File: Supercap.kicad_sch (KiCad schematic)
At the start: 2 parts

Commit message: more simulation work + fixed some things in root schematic
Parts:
- added V_{MiniPC}: Conn_01x02_Pin, symbol Connector:Conn_01x02_Pin
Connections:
- net Housekeeping/MiniPC: now also V_{MiniPC}.1 (Pin_1)
- new net GND: V_{MiniPC}.2 (Pin_2)
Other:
- sheet Control ports: added none; removed SCL_{IN}, SDA_{IN}
- sheet Housekeeping ports: added +12V; removed +5V
- sheet Voltage Converter ports: added +12V; removed +10V
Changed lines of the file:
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@@
-	)
-	(junction
-		(at 86.36 80.01)
-		(diameter 0)
-		(color 0 0 0 0)
 	)
 	(junction
@@
 		)
 	)
+	(wire
+		(pts
+			(xy 137.16 71.12) (xy 137.16 82.55)
+		)
+		(stroke
+			(width 0)
+			(type default)
+		)
+	)
 	(polyline
 		(pts
@@
 		)
 	)
+	(wire
+		(pts
+			(xy 35.56 82.55) (xy 35.56 85.09)
+		)
+		(stroke
+			(width 0)
+			(type default)
+		)
+	)
 	(polyline
 		(pts
@@
 	(wire
 		(pts
-			(xy 86.36 80.01) (xy 88.9 80.01)
+			(xy 82.55 82.55) (xy 88.9 82.55)
 		)
 		(stroke
@@
 	(wire
 		(pts
-			(xy 83.82 83.82) (xy 82.55 83.82)
-		)
-		(stroke
-			(width 0)
-			(type default)
-		)
-	)
-	(wire
-		(pts
 			(xy 205.74 57.15) (xy 205.74 60.96)
 		)
@@
 		)
 	)
+	(wire
+		(pts
+			(xy 33.02 80.01) (xy 40.64 80.01)
+		)
+		(stroke
+			(width 0)
+			(type default)
+		)
+	)
 	(polyline
 		(pts
@@
 	(wire
 		(pts
-			(xy 134.62 73.66) (xy 86.36 73.66)
-		)
-		(stroke
-			(width 0)
-			(type default)
-		)
-	)
-	(wire
-		(pts
-			(xy 82.55 80.01) (xy 86.36 80.01)
-		)
-		(stroke
-			(width 0)
-			(type default)
-		)
-	)
-	(wire
-		(pts
 			(xy 63.5 54.61) (xy 138.43 54.61)
 		)
@@
 		)
 	)
+	(wire
+		(pts
+			(xy 137.16 82.55) (xy 142.24 82.55)
+		)
+		(stroke
+			(width 0)
+			(type default)
+		)
+	)
 	(polyline
 		(pts
@@
 		)
 	)
+	(wire
+		(pts
+			(xy 33.02 82.55) (xy 35.56 82.55)
+		)
+		(stroke
+			(width 0)
+			(type default)
+		)
+	)
 	(polyline
 		(pts
@@
 		)
 	)
-	(wire
-		(pts
-			(xy 86.36 73.66) (xy 86.36 80.01)
-		)
-		(stroke
-			(width 0)
-			(type default)
-		)
-	)
 	(polyline
 		(pts
@@
 		)
 	)
+	(wire
+		(pts
+			(xy 85.09 71.12) (xy 137.16 71.12)
+		)
+		(stroke
+			(width 0)
+			(type default)
+		)
+	)
+	(wire
+		(pts
+			(xy 85.09 80.01) (xy 85.09 71.12)
+		)
+		(stroke
+			(width 0)
+			(type default)
+		)
+	)
+	(wire
+		(pts
+			(xy 82.55 80.01) (xy 85.09 80.01)
+		)
+		(stroke
+			(width 0)
+			(type default)
+		)
+	)
 	(polyline
 		(pts
@@
 			(width 0)
 			(type default)
-		)
-	)
-	(label "+5V"
-		(at 83.82 83.82 0)
-		(effects
-			(font
-				(size 1.27 1.27)
-			)
-			(justify left bottom)
 		)
 	)
@@
 	(symbol
 		(lib_id "Connector:Conn_01x02_Pin")
+		(at 27.94 80.01 0)
+		(unit 1)
+		(exclude_from_sim no)
+		(in_bom yes)
+		(on_board yes)
+		(dnp no)
+		(property "Reference" "V_{MiniPC}"
+			(at 19.685 79.756 0)
+			(effects
+				(font
+					(size 1.27 1.27)
+				)
+			)
+		)
+		(property "Value" "Conn_01x02_Pin"
+			(at 19.685 82.296 0)
+			(effects
+				(font
+					(size 1.27 1.27)
+				)
+			)
+		)
+		(property "Footprint" ""
+			(at 27.94 80.01 0)
+			(effects
+				(font
+					(size 1.27 1.27)
+				)
+				(hide yes)
+			)
+		)
+		(property "Datasheet" "~"
+			(at 27.94 80.01 0)
+			(effects
+				(font
+					(size 1.27 1.27)
+				)
+				(hide yes)
+			)
+		)
+		(property "Description" "Generic connector, single row, 01x02, script generated"
+			(at 27.94 80.01 0)
+			(effects
+				(font
+					(size 1.27 1.27)
+				)
+				(hide yes)
+			)
+		)
+		(pin "2"
+		)
+		(pin "1"
+		)
+		(instances
+			(project "Supercap"
+				(path "/98ee8313-37ab-4329-91ab-b5710476f82f"
+					(reference "V_{MiniPC}")
+					(unit 1)
+				)
+			)
+		)
+	)
+	(symbol
+		(lib_id "Connector:Conn_01x02_Pin")
 		(at 58.42 54.61 0)
 		(unit 1)
@@
 		)
 	)
+	(symbol
+		(lib_id "power:GND")
+		(at 35.56 85.09 0)
+		(unit 1)
+		(exclude_from_sim no)
+		(in_bom yes)
+		(on_board yes)
+		(dnp no)
+		(fields_autoplaced yes)
+		(property "Reference" "#PWR012"
+			(at 35.56 91.44 0)
+			(effects
+				(font
+					(size 1.27 1.27)
+				)
+				(hide yes)
+			)
+		)
+		(property "Value" "GND"
+			(at 35.56 90.17 0)
+			(effects
+				(font
+					(size 1.27 1.27)
+				)
+			)
+		)
+		(property "Footprint" ""
+			(at 35.56 85.09 0)
+			(effects
+				(font
+					(size 1.27 1.27)
+				)
+				(hide yes)
+			)
+		)
+		(property "Datasheet" ""
+			(at 35.56 85.09 0)
+			(effects
+				(font
+					(size 1.27 1.27)
+				)
+				(hide yes)
+			)
+		)
+		(property "Description" "Power symbol creates a global label with name \"GND\" , ground"
+			(at 35.56 85.09 0)
+			(effects
+				(font
+					(size 1.27 1.27)
+				)
+				(hide yes)
+			)
+		)
+		(pin "1"
+		)
+		(instances
+			(project ""
+				(path "/98ee8313-37ab-4329-91ab-b5710476f82f"
+					(reference "#PWR012")
+					(unit 1)
+				)
+			)
+		)
+	)
 	(sheet
 		(at 40.64 77.47)
@@
 		)
 		(pin "+3V3" output
+			(at 82.55 82.55 0)
+			(effects
+				(font
+					(size 1.27 1.27)
+				)
+				(justify right)
+			)
+		)
+		(pin "+12V" output
 			(at 82.55 80.01 0)
-			(effects
-				(font
-					(size 1.27 1.27)
-				)
-				(justify right)
-			)
-		)
-		(pin "+5V" output
-			(at 82.55 83.82 0)
 			(effects
 				(font
@@
 			)
 		)
-		(pin "+10V" input
+		(pin "+12V" input
 			(at 142.24 82.55 180)
 			(effects
@@
 			)
 		)
-		(pin "SDA_{IN}" bidirectional
-			(at 88.9 100.33 180)
-			(effects
-				(font
-					(size 1.27 1.27)
-				)
-				(justify left)
-			)
-		)
 		(pin "+3V3" input
-			(at 88.9 80.01 180)
-			(effects
-				(font
-					(size 1.27 1.27)
-				)
-				(justify left)
-			)
-		)
-		(pin "SCL_{IN}" input
-			(at 88.9 96.52 180)
-			(effects
-				(font
+			(at 88.9 82.55 180)
+			(effects
+				(font

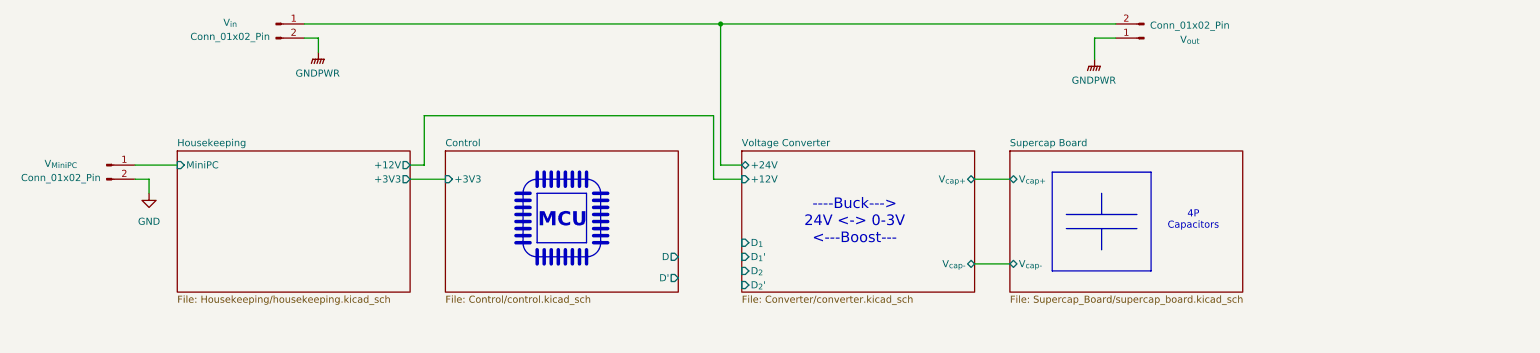
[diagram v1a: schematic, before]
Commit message: wiring connected, now only need msmp0 pinout and footprint assignments
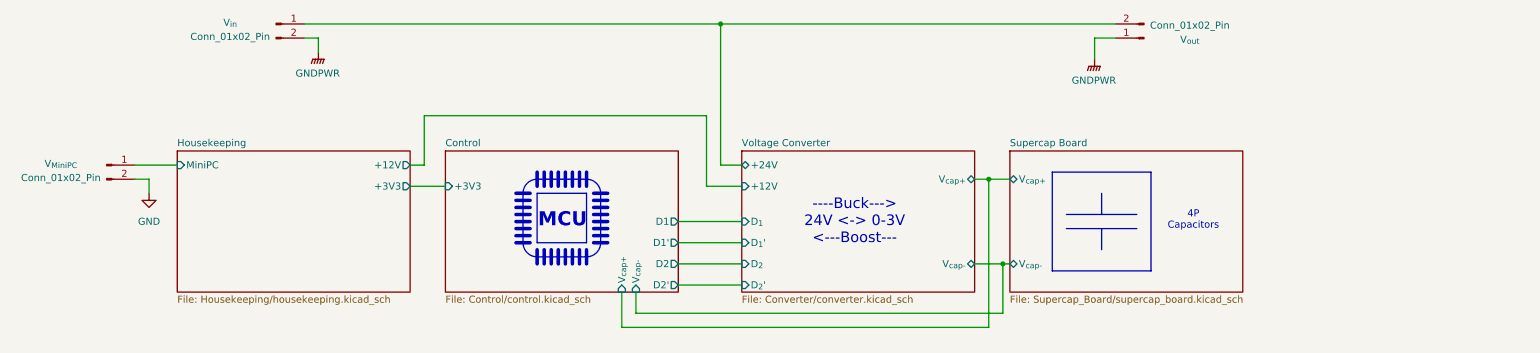
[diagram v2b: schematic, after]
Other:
- sheet Control ports: added D1, D1', D2, D2', V_{cap+}, V_{cap-}; removed D, D'
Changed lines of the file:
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@@
+	)
+	(junction
+		(at 186.69 82.55)
+		(diameter 0)
+		(color 0 0 0 0)
+	)
+	(junction
+		(at 189.23 97.79)
+		(diameter 0)
+		(color 0 0 0 0)
 	)
 	(junction
@@
 		(color 0 0 0 0)
 	)
+	(wire
+		(pts
+			(xy 120.65 102.87) (xy 120.65 109.22)
+		)
+		(stroke
+			(width 0)
+			(type default)
+		)
+	)
 	(polyline
 		(pts
@@
 	(wire
 		(pts
+			(xy 186.69 109.22) (xy 186.69 82.55)
+		)
+		(stroke
+			(width 0)
+			(type default)
+		)
+	)
+	(wire
+		(pts
 			(xy 209.55 57.15) (xy 205.74 57.15)
 		)
@@
 	(wire
 		(pts
-			(xy 137.16 71.12) (xy 137.16 82.55)
+			(xy 135.89 71.12) (xy 135.89 83.82)
 		)
 		(stroke
@@
 	(wire
 		(pts
-			(xy 82.55 82.55) (xy 88.9 82.55)
+			(xy 82.55 83.82) (xy 88.9 83.82)
 		)
 		(stroke
@@
 	(wire
 		(pts
+			(xy 130.81 90.17) (xy 142.24 90.17)
+		)
+		(stroke
+			(width 0)
+			(type default)
+		)
+	)
+	(wire
+		(pts
+			(xy 130.81 97.79) (xy 142.24 97.79)
+		)
+		(stroke
+			(width 0)
+			(type default)
+		)
+	)
+	(wire
+		(pts
 			(xy 205.74 57.15) (xy 205.74 60.96)
 		)
@@
 		)
 	)
+	(wire
+		(pts
+			(xy 120.65 109.22) (xy 186.69 109.22)
+		)
+		(stroke
+			(width 0)
+			(type default)
+		)
+	)
 	(polyline
 		(pts
@@
 		)
 	)
+	(wire
+		(pts
+			(xy 123.19 106.68) (xy 189.23 106.68)
+		)
+		(stroke
+			(width 0)
+			(type default)
+		)
+	)
 	(polyline
 		(pts
@@
 	(wire
 		(pts
-			(xy 184.15 97.79) (xy 190.5 97.79)
+			(xy 184.15 97.79) (xy 189.23 97.79)
 		)
 		(stroke
@@
 	(wire
 		(pts
-			(xy 137.16 82.55) (xy 142.24 82.55)
+			(xy 135.89 83.82) (xy 142.24 83.82)
 		)
 		(stroke
@@
 	(wire
 		(pts
-			(xy 184.15 82.55) (xy 190.5 82.55)
+			(xy 184.15 82.55) (xy 186.69 82.55)
 		)
 		(stroke
@@
 		)
 	)
+	(wire
+		(pts
+			(xy 123.19 102.87) (xy 123.19 106.68)
+		)
+		(stroke
+			(width 0)
+			(type default)
+		)
+	)
 	(polyline
 		(pts
@@
 		)
 	)
+	(wire
+		(pts
+			(xy 130.81 101.6) (xy 142.24 101.6)
+		)
+		(stroke
+			(width 0)
+			(type default)
+		)
+	)
 	(polyline
 		(pts
@@
 		)
 	)
+	(wire
+		(pts
+			(xy 130.81 93.98) (xy 142.24 93.98)
+		)
+		(stroke
+			(width 0)
+			(type default)
+		)
+	)
+	(wire
+		(pts
+			(xy 189.23 106.68) (xy 189.23 97.79)
+		)
+		(stroke
+			(width 0)
+			(type default)
+		)
+	)
 	(polyline
 		(pts
@@
 	(wire
 		(pts
+			(xy 186.69 82.55) (xy 190.5 82.55)
+		)
+		(stroke
+			(width 0)
+			(type default)
+		)
+	)
+	(wire
+		(pts
 			(xy 33.02 82.55) (xy 35.56 82.55)
 		)
@@
 	(wire
 		(pts
-			(xy 85.09 71.12) (xy 137.16 71.12)
+			(xy 85.09 71.12) (xy 135.89 71.12)
 		)
 		(stroke
@@
 		(pts
 			(xy 138.43 54.61) (xy 209.55 54.61)
+		)
+		(stroke
+			(width 0)
+			(type default)
+		)
+	)
+	(wire
+		(pts
+			(xy 189.23 97.79) (xy 190.5 97.79)
 		)
 		(stroke
@@
 		)
 		(pin "+3V3" output
-			(at 82.55 82.55 0)
+			(at 82.55 83.82 0)
 			(effects
 				(font
@@
 		)
 		(pin "+12V" input
-			(at 142.24 82.55 180)
+			(at 142.24 83.82 180)
 			(effects
 				(font
@@
 		)
 		(pin "D_{1}" input
+			(at 142.24 90.17 180)
+			(effects
+				(font
+					(size 1.27 1.27)
+				)
+				(justify left)
+			)
+		)
+		(pin "D_{1}'" input
 			(at 142.24 93.98 180)
 			(effects
@@
 			)
 		)
-		(pin "D_{1}'" input
-			(at 142.24 96.52 180)
-			(effects
-				(font
-					(size 1.27 1.27)
-				)
-				(justify left)
-			)
-		)
 		(pin "D_{2}" input
-			(at 142.24 99.06 180)
+			(at 142.24 97.79 180)
 			(effects
 				(font
@@
 		)
 		(pin "+3V3" input
-			(at 88.9 82.55 180)
+			(at 88.9 83.82 180)
 			(effects
 				(font
@@
 			)
 		)
-		(pin "D" output
-			(at 130.81 96.52 0)
+		(pin "D1" output
+			(at 130.81 90.17 0)
 			(effects
 				(font
@@
 			)
 		)
-		(pin "D'" output
-			(at 130.81 100.33 0)
+		(pin "D1'" output
+			(at 130.81 93.98 0)
 			(effects
 				(font
@@
 			)
 		)
+		(pin "D2" output
+			(at 130.81 97.79 0)
+			(effects
+				(font
+					(size 1.27 1.27)
+				)
+				(justify right)
+			)
+		)
+		(pin "D2'" output
+			(at 130.81 101.6 0)
+			(effects
+				(font
+					(size 1.27 1.27)
+				)
+				(justify right)
+			)
+		)
+		(pin "V_{cap+}" input
+			(at 120.65 102.87 270)
+			(effects
+				(font
+					(size 1.27 1.27)
+				)
+				(justify left)
+			)
+		)
+		(pin "V_{cap-}" input
+			(at 123.19 102.87 270)
+			(effects
+				(font
+					(size 1.27 1.27)
+				)
+				(justify left)
+			)
+		)

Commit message: removed v1 files and assigned mouser part numbers
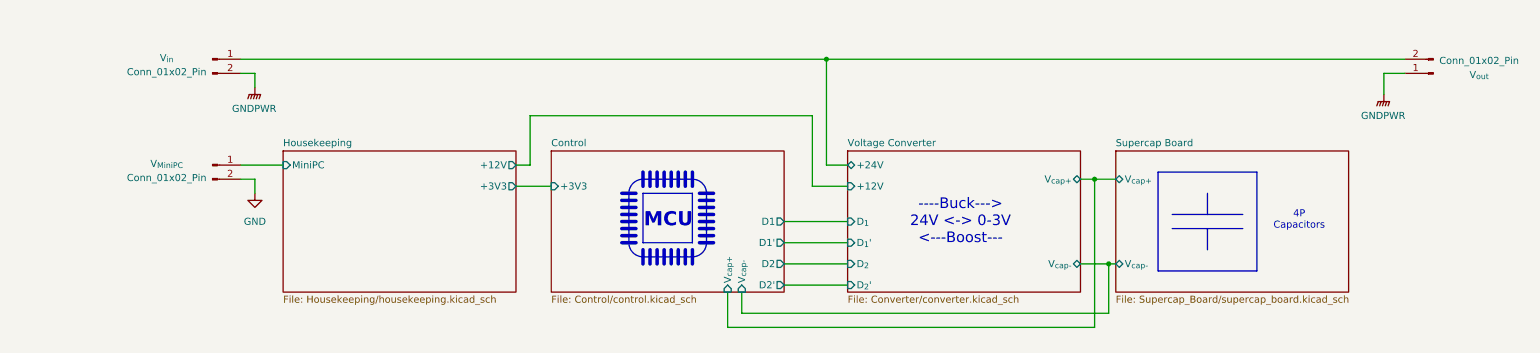
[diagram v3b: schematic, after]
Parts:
- V_{MiniPC}, V_{in}, V_{out}: footprint (none) -> Connector_AMASS:AMASS_XT30U-F_1x02_P5.0mm_Vertical; now left out of the parts list
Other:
- moved on the sheet: V_{MiniPC}, V_{in}, V_{out}

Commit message: began layout
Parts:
- renumbered V_{MiniPC} to V_{MiniPC}1, V_{in} to V_{in}1, V_{out} to V_{out}1
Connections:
- net Voltage Converter/+24V renamed Control/I_{bat,in+}
- net Control/I_{bat,in+}: no longer V_{out}1.2 (Pin_2)
- new net Control/I_{bat,out+}: V_{out}1.2 (Pin_2)
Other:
- sheet Control ports: added I_{L,out+}, I_{bat,in+}, I_{bat,out+}, V_{sc,+}, V_{sc,-}; removed V_{cap+}, V_{cap-}
- moved on the sheet: V_{MiniPC}1, V_{in}1, V_{out}1

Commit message: mostly done with first order layout
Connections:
- net Control/I_{bat,in+}: now also V_{in}1.2 (Pin_2); no longer V_{in}1.1 (Pin_1)
- net GNDPWR: now also V_{in}1.1 (Pin_1); no longer V_{in}1.2 (Pin_2)
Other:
- sheet Housekeeping ports: added +24V; removed none
- company: (none) -> UT Robomaster
- moved on the sheet: V_{MiniPC}1
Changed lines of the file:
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@@
 	(generator_version "9.0")
 	(paper "A4")
+	(title_block
+		(company "UT Robomaster")
+		(comment 1 "Robomaster")
+	)
 	(arc
 		(start 119.38 96.52)
@@
 	)
 	(junction
+		(at 67.31 60.96)
+		(diameter 0)
+		(color 0 0 0 0)
+	)
+	(junction
 		(at 205.74 97.79)
 		(diameter 0)
@@
 	(wire
 		(pts
-			(xy 59.69 60.96) (xy 97.79 60.96)
+			(xy 59.69 60.96) (xy 67.31 60.96)
 		)
 		(stroke
@@
 	(wire
 		(pts
-			(xy 45.72 82.55) (xy 45.72 85.09)
+			(xy 45.72 85.09) (xy 45.72 87.63)
 		)
 		(stroke
@@
 	(wire
 		(pts
-			(xy 43.18 80.01) (xy 50.8 80.01)
+			(xy 43.18 82.55) (xy 50.8 82.55)
+		)
+		(stroke
+			(width 0)
+			(type default)
+		)
+	)
+	(wire
+		(pts
+			(xy 50.8 80.01) (xy 48.26 80.01)
 		)
 		(stroke
@@
 		)
 	)
+	(wire
+		(pts
+			(xy 67.31 60.96) (xy 97.79 60.96)
+		)
+		(stroke
+			(width 0)
+			(type default)
+		)
+	)
 	(polyline
 		(pts
@@
 		)
 	)
+	(wire
+		(pts
+			(xy 48.26 73.66) (xy 67.31 73.66)
+		)
+		(stroke
+			(width 0)
+			(type default)
+		)
+	)
 	(polyline
 		(pts
@@
 	(wire
 		(pts
+			(xy 67.31 60.96) (xy 67.31 73.66)
+		)
+		(stroke
+			(width 0)
+			(type default)
+		)
+	)
+	(wire
+		(pts
 			(xy 205.74 97.79) (xy 208.28 97.79)
 		)
@@
 	(wire
 		(pts
-			(xy 43.18 82.55) (xy 45.72 82.55)
+			(xy 43.18 85.09) (xy 45.72 85.09)
 		)
 		(stroke
@@
 		(pts
 			(xy 144.78 100.33) (xy 148.59 100.33)
+		)
+		(stroke
+			(width 0)
+			(type default)
+		)
+	)
+	(wire
+		(pts
+			(xy 48.26 80.01) (xy 48.26 73.66)
 		)
 		(stroke
@@
 	(symbol
 		(lib_id "Connector:Conn_01x02_Pin")
-		(at 38.1 80.01 0)
+		(at 38.1 82.55 0)
 		(unit 1)
 		(exclude_from_sim no)
@@
 		(dnp no)
 		(property "Reference" "V_{MiniPC}1"
-			(at 29.845 79.756 0)
+			(at 29.845 82.296 0)
 			(effects
 				(font
@@
 		)
 		(property "Value" "Conn_01x02_Pin"
-			(at 29.845 82.296 0)
+			(at 29.845 84.836 0)
 			(effects
 				(font
@@
 		)
 		(property "Footprint" "Connector_AMASS:AMASS_XT30U-F_1x02_P5.0mm_Vertical"
-			(at 38.1 80.01 0)
+			(at 38.1 82.55 0)
 			(effects
 				(font
@@
 		)
 		(property "Datasheet" "~"
-			(at 38.1 80.01 0)
+			(at 38.1 82.55 0)
 			(effects
 				(font
@@
 		)
 		(property "Description" "Generic connector, single row, 01x02, script generated"
-			(at 38.1 80.01 0)
+			(at 38.1 82.55 0)
 			(effects
 				(font
@@
 	(symbol
 		(lib_id "Connector:Conn_01x02_Pin")
-		(at 54.61 60.96 0)
+		(at 54.61 63.5 0)
+		(mirror x)
 		(unit 1)
 		(exclude_from_sim no)
@@
 		(dnp no)
 		(property "Reference" "V_{in}1"
-			(at 46.355 60.706 0)
+			(at 46.355 63.754 0)
 			(effects
 				(font
@@
 		)
 		(property "Value" "Conn_01x02_Pin"
-			(at 46.355 63.246 0)
+			(at 46.355 61.214 0)
 			(effects
 				(font
@@
 		)
 		(property "Footprint" "Connector_AMASS:AMASS_XT30U-F_1x02_P5.0mm_Vertical"
-			(at 54.61 60.96 0)
+			(at 54.61 63.5 0)
 			(effects
 				(font
@@
 		)
 		(property "Datasheet" "~"
-			(at 54.61 60.96 0)
+			(at 54.61 63.5 0)
 			(effects
 				(font
@@
 		)
 		(property "Description" "Generic connector, single row, 01x02, script generated"
-			(at 54.61 60.96 0)
+			(at 54.61 63.5 0)
 			(effects
 				(font
@@
 	(symbol
 		(lib_id "power:GND")
-		(at 45.72 85.09 0)
+		(at 45.72 87.63 0)
 		(unit 1)
 		(exclude_from_sim no)
@@
 		(fields_autoplaced yes)
 		(property "Reference" "#PWR01"
-			(at 45.72 91.44 0)
+			(at 45.72 93.98 0)
 			(effects
 				(font
@@
 		)
 		(property "Value" "GND"
-			(at 45.72 90.17 0)
+			(at 45.72 92.71 0)
 			(effects
 				(font
@@
 		)
 		(property "Footprint" ""
-			(at 45.72 85.09 0)
+			(at 45.72 87.63 0)
 			(effects
 				(font
@@
 		)
 		(property "Datasheet" ""
-			(at 45.72 85.09 0)
+			(at 45.72 87.63 0)
 			(effects
 				(font
@@
 		)
 		(property "Description" "Power symbol creates a global label with name \"GND\" , ground"
-			(at 45.72 85.09 0)
+			(at 45.72 87.63 0)
 			(effects
 				(font
@@
 		)
 		(pin "MiniPC" input
+			(at 50.8 82.55 180)
+			(effects
+				(font
+					(size 1.27 1.27)
+				)
+				(justify left)
+			)
+		)
+		(pin "+24V" input
 			(at 50.8 80.01 180)
 			(effects

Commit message: ok hopefully this doesnt break everything, committing after doing in kicadlib submod
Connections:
- net Control/I_{bat,out+} renamed I_{out sense-}
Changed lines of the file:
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@@
+	(wire
+		(pts
+			(xy 133.35 66.04) (xy 208.28 66.04)
+		)
+		(stroke
+			(width 0)
+			(type default)
+		)
+	)
 	(wire
 		(pts
@@
 		)
 	)
+	(wire
+		(pts
+			(xy 135.89 77.47) (xy 135.89 68.58)
+		)
+		(stroke
+			(width 0)
+			(type default)
+		)
+	)
 	(polyline
 		(pts
@@
 		)
 	)
+	(wire
+		(pts
+			(xy 212.09 68.58) (xy 212.09 60.96)
+		)
+		(stroke
+			(width 0)
+			(type default)
+		)
+	)
 	(polyline
 		(pts
@@
 	(wire
 		(pts
+			(xy 135.89 68.58) (xy 212.09 68.58)
+		)
+		(stroke
+			(width 0)
+			(type default)
+		)
+	)
+	(wire
+		(pts
 			(xy 198.12 97.79) (xy 205.74 97.79)
 		)
@@
 		)
 	)
+	(wire
+		(pts
+			(xy 133.35 77.47) (xy 133.35 66.04)
+		)
+		(stroke
+			(width 0)
+			(type default)
+		)
+	)
 	(polyline
 		(pts
@@
 		)
 	)
+	(wire
+		(pts
+			(xy 208.28 66.04) (xy 208.28 60.96)
+		)
+		(stroke
+			(width 0)
+			(type default)
+		)
+	)
 	(polyline
 		(pts
@@
 	(wire
 		(pts
+			(xy 212.09 60.96) (xy 232.41 60.96)
+		)
+		(stroke
+			(width 0)
+			(type default)
+		)
+	)
+	(wire
+		(pts
 			(xy 148.59 111.76) (xy 205.74 111.76)
 		)
@@
 	(wire
 		(pts
-			(xy 177.8 60.96) (xy 232.41 60.96)
+			(xy 177.8 60.96) (xy 208.28 60.96)
 		)
 		(stroke
@@
 		)
 	)
+	(hierarchical_label "I_{out sense-}"
+		(shape input)
+		(at 135.89 77.47 270)
+		(effects
+			(font
+				(size 1.27 1.27)
+			)
+			(justify right)
+		)
+	)
+	(hierarchical_label "I_{out sense+}"
+		(shape input)
+		(at 133.35 77.47 270)
+		(effects
+			(font
+				(size 1.27 1.27)
+			)
+			(justify right)
+		)
+	)

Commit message: added mspm0 fp, still need to map pin nets on sym in schematic, in process of doing redesign to min power path
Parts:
- V_{MiniPC}1, V_{in}1, V_{out}1: footprint Connector_AMASS:AMASS_XT30U-F_1x02_P5.0mm_Vertical -> Connector_AMASS:AMASS_XT30PW-F_1x02_P2.50mm_Horizontal
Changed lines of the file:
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@@
 			)
 		)
-		(property "Footprint" "Connector_AMASS:AMASS_XT30U-F_1x02_P5.0mm_Vertical"
+		(property "Footprint" "Connector_AMASS:AMASS_XT30PW-F_1x02_P2.50mm_Horizontal"
 			(at 38.1 82.55 0)
 			(effects
@@
 			)
 		)
-		(property "Footprint" "Connector_AMASS:AMASS_XT30U-F_1x02_P5.0mm_Vertical"
+		(property "Footprint" "Connector_AMASS:AMASS_XT30PW-F_1x02_P2.50mm_Horizontal"
 			(at 54.61 63.5 0)
 			(effects
@@
 			)
 		)
-		(property "Footprint" "Connector_AMASS:AMASS_XT30U-F_1x02_P5.0mm_Vertical"
+		(property "Footprint" "Connector_AMASS:AMASS_XT30PW-F_1x02_P2.50mm_Horizontal"
 			(at 237.49 63.5 0)
 			(effects

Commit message: via stitching on fets, fixed sheet pin (not label on parent) for isense, messed around with design
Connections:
- net I_{out sense-} renamed Control/I_{out sense-}
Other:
- sheet Control ports: added I_{out sense+}, I_{out sense-}; removed none
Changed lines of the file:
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@@
-		)
-	)
-	(hierarchical_label "I_{out sense-}"
-		(shape input)
-		(at 135.89 77.47 270)
-		(effects
-			(font
-				(size 1.27 1.27)
-			)
-			(justify right)
-		)
-	)
-	(hierarchical_label "I_{out sense+}"
-		(shape input)
-		(at 133.35 77.47 270)
-		(effects
-			(font
-				(size 1.27 1.27)
-			)
-			(justify right)
 		)
 	)
@@
 			(effects
 				(font
+					(size 1.27 1.27)
+				)
+				(justify right)
+			)
+		)
+		(pin "I_{out sense+}" bidirectional
+			(at 133.35 77.47 90)
+			(effects
+				(font
+					(size 1.27 1.27)
+				)
+				(justify right)
+			)
+		)
+		(pin "I_{out sense-}" bidirectional
+			(at 135.89 77.47 90)
+			(effects
+				(font
